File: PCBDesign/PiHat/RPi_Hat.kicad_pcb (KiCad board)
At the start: 2 copper layers, 65 x 56.5 mm, 5 parts, among them J2 RPi_GPIO

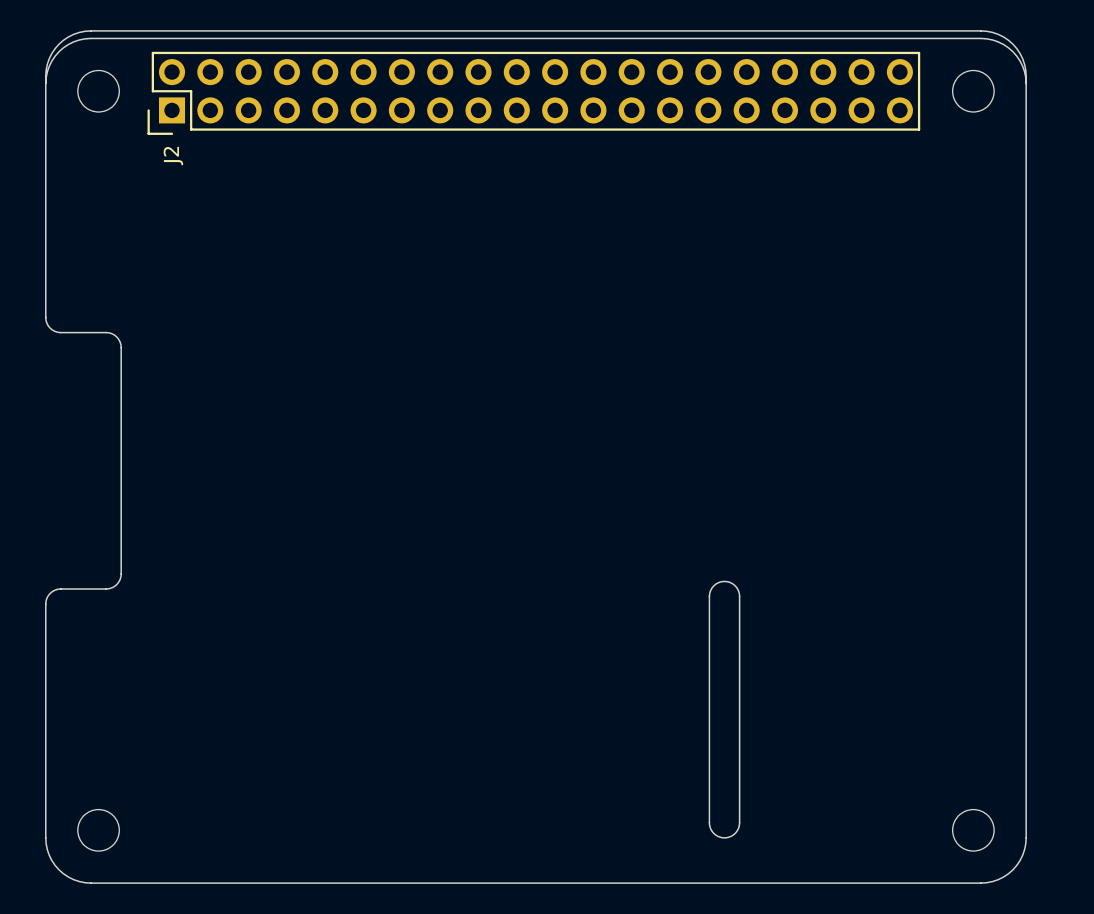
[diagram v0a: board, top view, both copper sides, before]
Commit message: First design, PiHat too small for our parts
Could possibly extend one side over the Pi
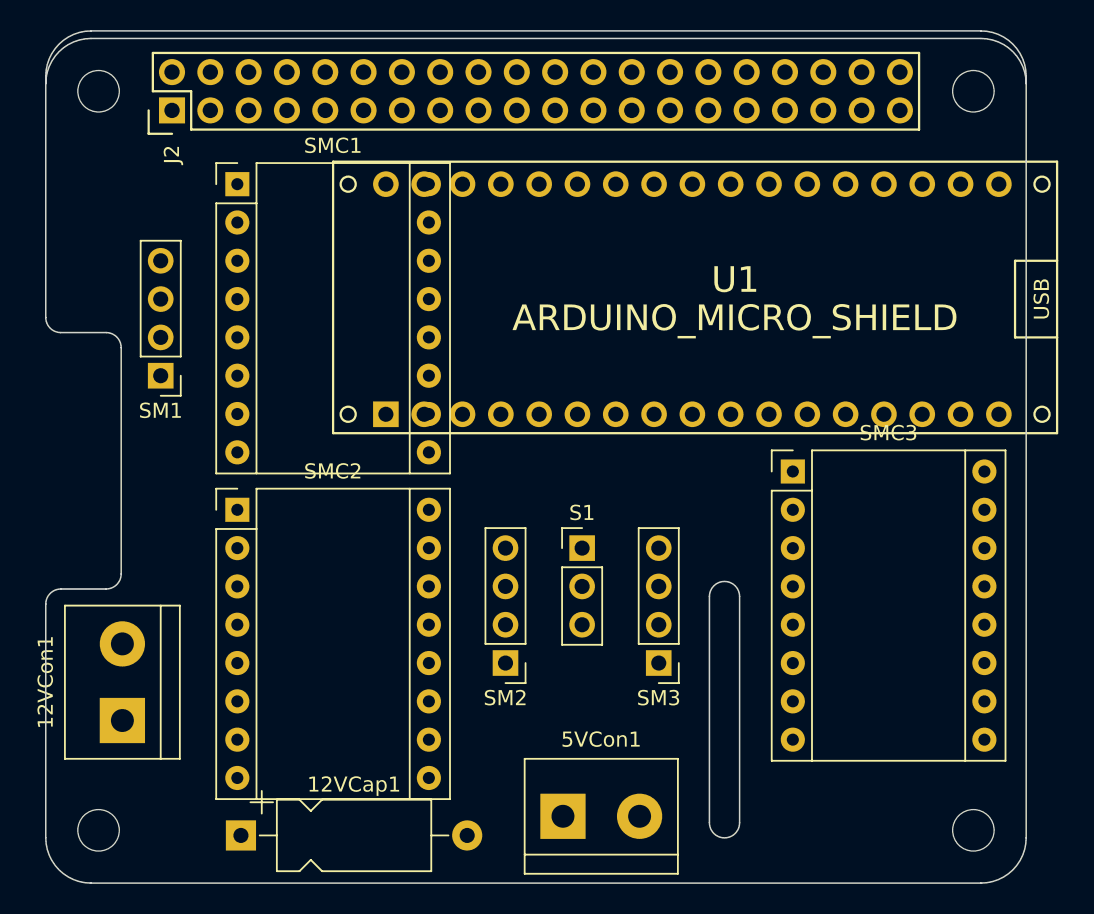
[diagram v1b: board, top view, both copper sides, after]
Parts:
- added 12VCap1: CAP, Capacitor_THT:CP_Axial_L10.0mm_D4.5mm_P15.00mm_Horizontal, F.Cu at (12.9, 53.3)
- added 12VCon1: Screw_Terminal_01x02, TerminalBlock:TerminalBlock_bornier-2_P5.08mm, F.Cu at (5.08, 45.7)
- added 5VCon1: Screw_Terminal_01x02, TerminalBlock:TerminalBlock_bornier-2_P5.08mm, F.Cu at (34.3, 52.1)
- added S1: Conn_01x03_Male, Connector_PinHeader_2.54mm:PinHeader_1x03_P2.54mm_Vertical, F.Cu at (35.6, 34.3)
- added SM1: Conn_01x04_Male, Connector_PinHeader_2.54mm:PinHeader_1x04_P2.54mm_Vertical, F.Cu at (7.62, 22.9)
- added SM2: Conn_01x04_Male, Connector_PinHeader_2.54mm:PinHeader_1x04_P2.54mm_Vertical, F.Cu at (30.5, 41.9)
- added SM3: Conn_01x04_Male, Connector_PinHeader_2.54mm:PinHeader_1x04_P2.54mm_Vertical, F.Cu at (40.6, 41.9)
- added SMC1: Pololu_Breakout_A4988, Module:Pololu_Breakout-16_15.2x20.3mm, F.Cu at (12.7, 10.2)
- added SMC2: Pololu_Breakout_A4988, Module:Pololu_Breakout-16_15.2x20.3mm, F.Cu at (12.7, 31.8)
- added SMC3: Pololu_Breakout_A4988, Module:Pololu_Breakout-16_15.2x20.3mm, F.Cu at (49.5, 29.2)
- added U1: ARDUINO_MICRO_SHIELD, arduino_micro_shield:ARDUINO_MICRO_SHIELD, F.Cu at (19.1, 26.7)
- J2: footprint RPi_Hat:Pin_Header_Straight_2x20 -> PiHat:Pin_Header_Straight_2x20
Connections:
- J2 pad 2: Net-(J2-Pad2) -> /RPi_GPIO/5V
- J2 pad 39: Net-(J2-Pad39) -> /RPi_GPIO/GND

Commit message: Minor fixes, started on traces
Part placement and Nano pins may need to be adjusted. Still missing: MMC and encoder schematic connections, IMU footprint and schematic connections
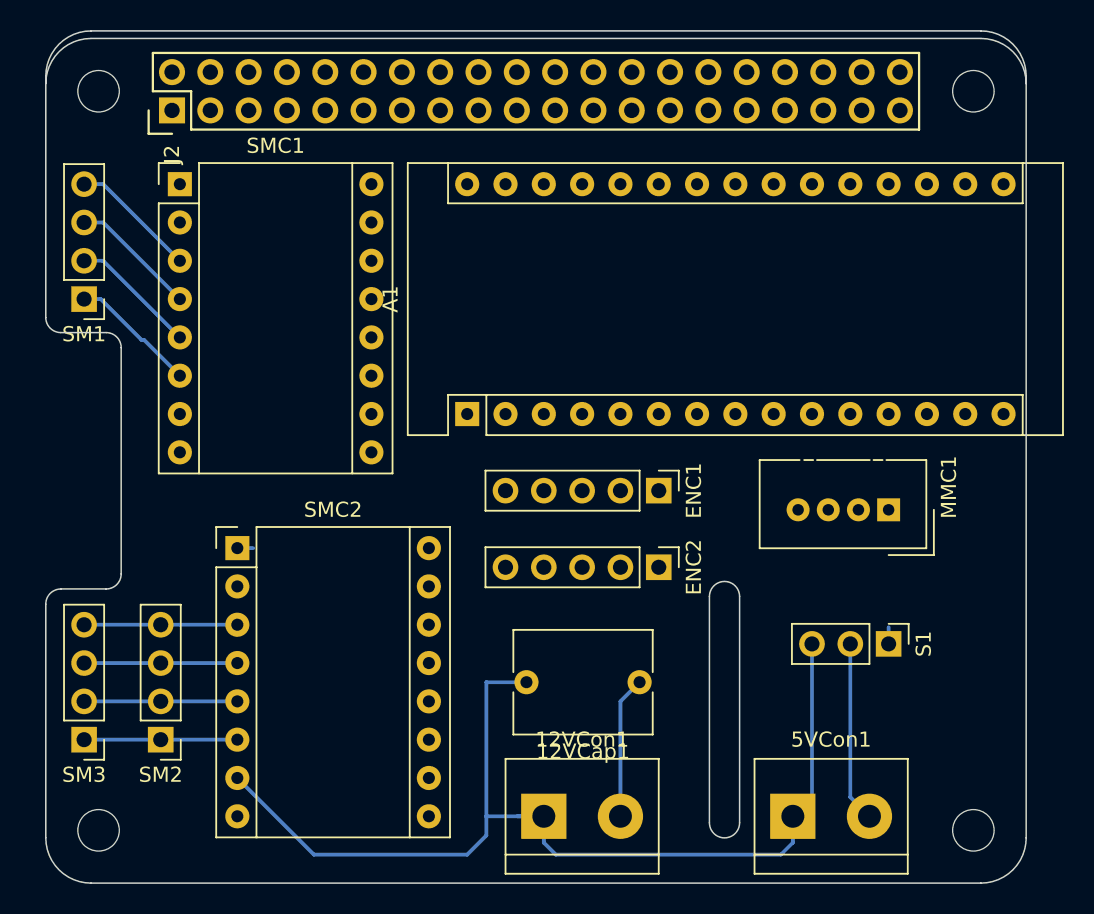
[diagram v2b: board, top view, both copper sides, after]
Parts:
- removed SMC3: Pololu_Breakout_A4988, Module:Pololu_Breakout-16_15.2x20.3mm
- removed U1: ARDUINO_MICRO_SHIELD, arduino_micro_shield:ARDUINO_MICRO_SHIELD
- added A1: Arduino_Nano_v3.x, Module:Arduino_Nano, F.Cu at (27.9, 25.4)
- added ENC1: Conn_01x05_Male, Connector_PinHeader_2.54mm:PinHeader_1x05_P2.54mm_Vertical, F.Cu at (40.6, 30.5)
- added ENC2: Conn_01x05_Male, Connector_PinHeader_2.54mm:PinHeader_1x05_P2.54mm_Vertical, F.Cu at (40.6, 35.6)
- added MMC1: Conn_01x04_Male, Connector:NS-Tech_Grove_1x04_P2mm_Vertical, F.Cu at (55.9, 31.8)
- 12VCap1: footprint Capacitor_THT:CP_Axial_L10.0mm_D4.5mm_P15.00mm_Horizontal -> Capacitor_THT:C_Rect_L9.0mm_W6.7mm_P7.50mm_MKT
- moved SM3 38.4 mm to (2.54, 47.0)
- moved 12VCon1 28.7 mm to (33.0, 52.1), turned to 0 degrees
- moved 12VCap1 28.3 mm to (39.4, 43.2), turned to 180 degrees
- moved SM2 23.4 mm to (7.62, 47.0)
- moved S1 21.3 mm to (55.9, 40.6), turned to 270 degrees
- moved 5VCon1 15.2 mm to (49.5, 52.1)
- moved SM1 7.18 mm to (2.54, 17.8)
- moved SMC1 3.81 mm to (8.89, 10.2)
- moved SMC2 2.54 mm to (12.7, 34.3)
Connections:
- SM3 pad 1: Net-(SM3-Pad1) -> Net-(SM2-Pad1)
- SM3 pad 2: Net-(SM3-Pad2) -> Net-(SM2-Pad2)
- SM3 pad 3: Net-(SM3-Pad3) -> Net-(SM2-Pad3)
- SM3 pad 4: Net-(SM3-Pad4) -> Net-(SM2-Pad4)
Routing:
- net /RPi_GPIO/GND: track 0.00 -> 71.2 mm
- net /RPi_GPIO/5V: track 0.00 -> 12.0 mm
- net Net-(SM2-Pad4): track 0.00 -> 10.2 mm
- net Net-(SM2-Pad3): track 0.00 -> 10.2 mm
- net Net-(SM2-Pad2): track 0.00 -> 10.2 mm
- net Net-(SM2-Pad1): track 0.00 -> 10.2 mm
- net /RPi_GPIO/12V: track 0.00 -> 9.42 mm
- net Net-(SM1-Pad3): track 0.00 -> 8.45 mm
- net Net-(SM1-Pad4): track 0.00 -> 8.45 mm
- net Net-(SM1-Pad2): track 0.00 -> 8.45 mm
- net Net-(SM1-Pad1): track 0.00 -> 8.45 mm
- net Net-(A1-Pad6): track 0.00 -> 1.10 mm
